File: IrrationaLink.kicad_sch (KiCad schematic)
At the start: 27 parts, among them J1 USB_C_Receptacle_USB2.0, U1 ESP32-C3, U2 LM2937xMP

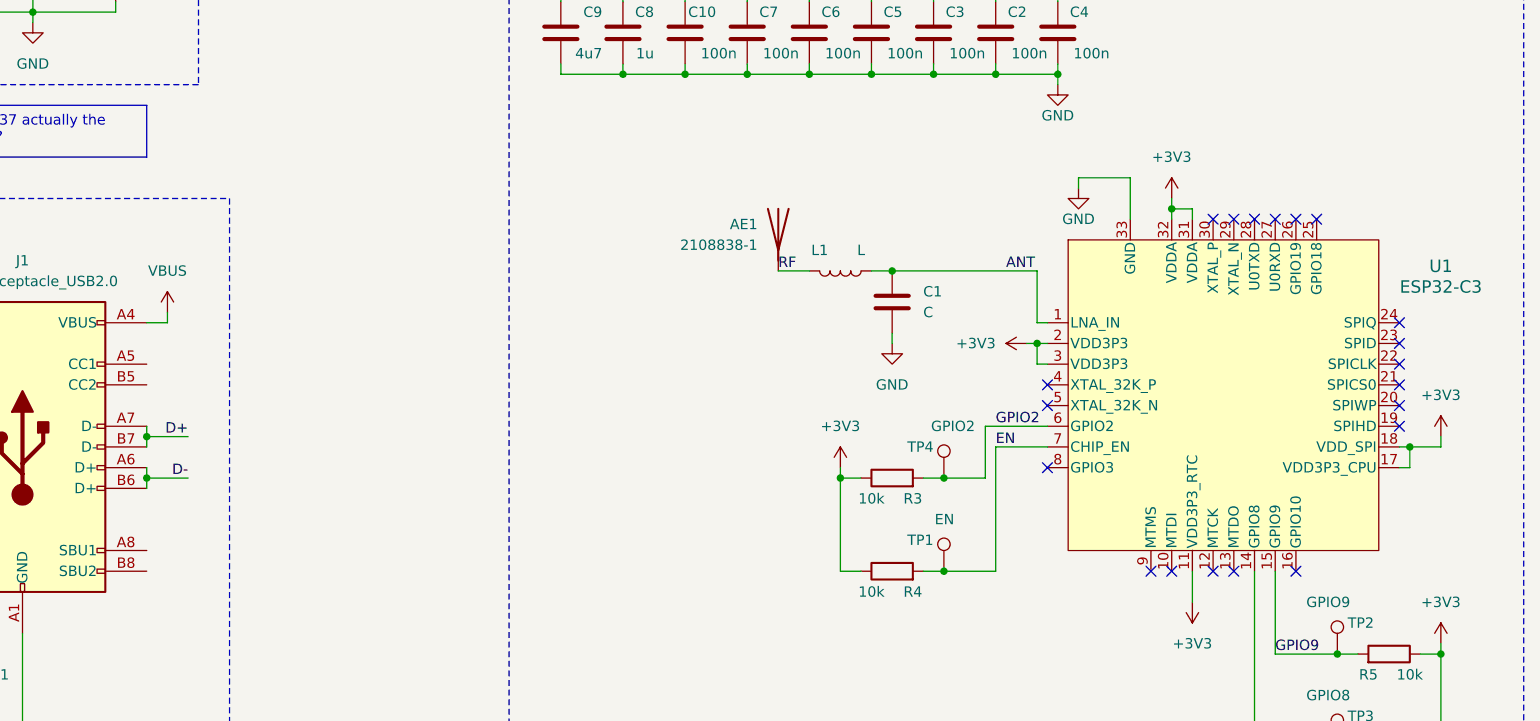
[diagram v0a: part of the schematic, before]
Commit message: Add gitignore; Route USB lines
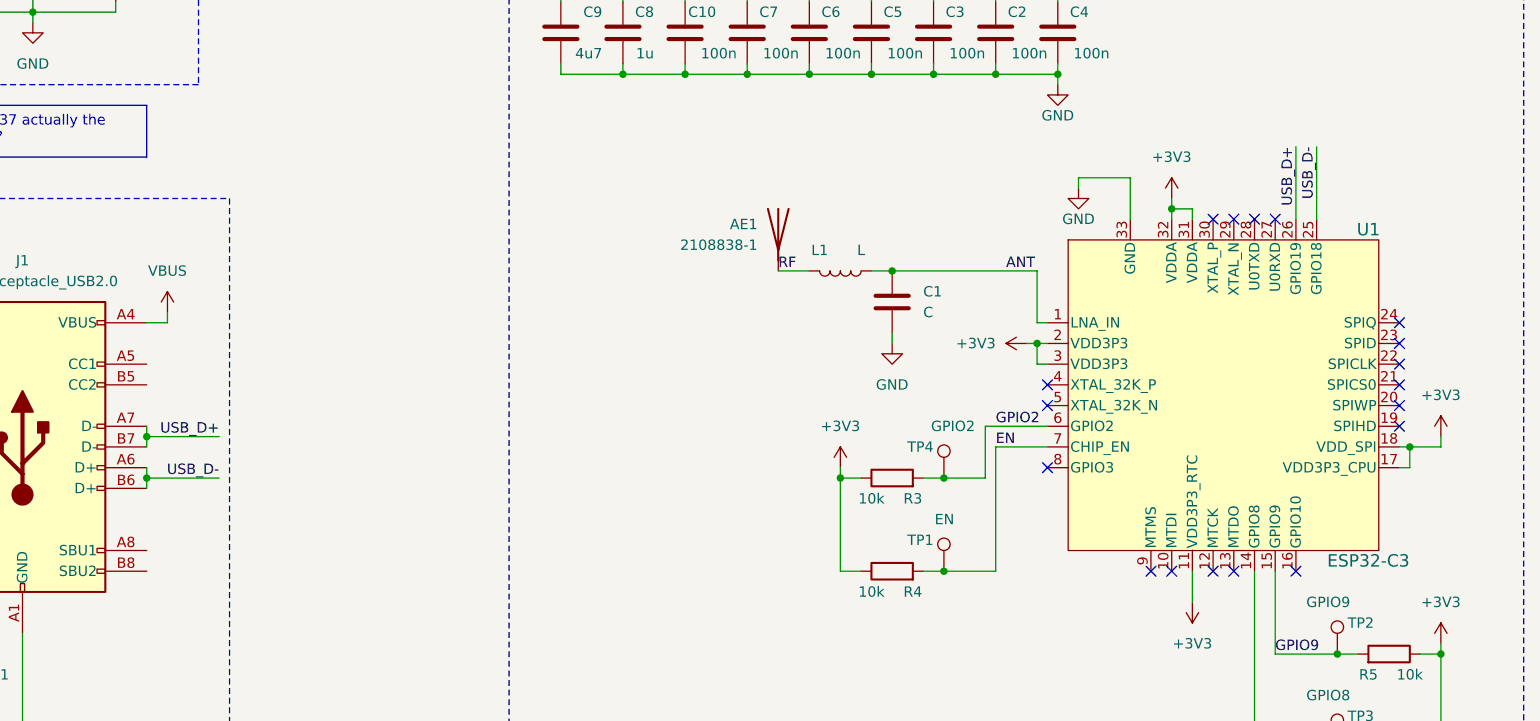
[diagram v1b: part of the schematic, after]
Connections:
- net D+ is gone; now on net USB_D+: J1.A7 (D-), J1.B7 (D-)
- net D- is gone; now on net USB_D-: J1.A6 (D+), J1.B6 (D+)
- net USB_D-: now reaches U1.25 (GPIO18)
- net USB_D+: now reaches U1.26 (GPIO19)
- no-connect marks 20 -> 18
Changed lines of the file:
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@@
   )
   (no_connect (at 233.68 86.36))
-  (no_connect (at 220.98 71.12))
   (no_connect (at 205.74 114.3))
   (no_connect (at 233.68 91.44))
@@
   (no_connect (at 190.5 93.98))
   (no_connect (at 233.68 83.82))
-  (no_connect (at 223.52 71.12))
   (wire (pts (xy 161.29 43.18) (xy 161.29 44.45))
     (stroke (width 0) (type default))
@@
     (stroke (width 0) (type default))
   )
-  (wire (pts (xy 80.01 102.87) (xy 85.09 102.87))
+  (wire (pts (xy 80.01 102.87) (xy 88.9 102.87))
     (stroke (width 0) (type default))
   )
@@
     (stroke (width 0) (type default))
   )
-  (wire (pts (xy 80.01 97.79) (xy 85.09 97.79))
+  (wire (pts (xy 80.01 97.79) (xy 88.9 97.79))
     (stroke (width 0) (type default))
   )
@@
     (stroke (width 0) (type default))
   )
+  (wire (pts (xy 223.52 62.23) (xy 223.52 71.12))
+    (stroke (width 0) (type default))
+  )
   (wire (pts (xy 146.05 43.18) (xy 138.43 43.18))
     (stroke (width 0) (type default))
@@
   )
   (wire (pts (xy 55.88 45.72) (xy 66.04 45.72))
+    (stroke (width 0) (type default))
+  )
+  (wire (pts (xy 220.98 62.23) (xy 220.98 71.12))
     (stroke (width 0) (type default))
   )
@@
     (effects (font (size 1.27 1.27)) (justify left bottom))
   )
-  (label "D-" (at 85.09 102.87 180) (fields_autoplaced)
+  (label "USB_D-" (at 88.9 102.87 180) (fields_autoplaced)
     (effects (font (size 1.27 1.27)) (justify right bottom))
   )
@@
     (effects (font (size 1.27 1.27)) (justify left bottom))
   )
-  (label "D+" (at 85.09 97.79 180) (fields_autoplaced)
+  (label "USB_D+" (at 88.9 97.79 180) (fields_autoplaced)
     (effects (font (size 1.27 1.27)) (justify right bottom))
   )
@@
     (effects (font (size 1.27 1.27)) (justify right bottom))
   )
+  (label "USB_D+" (at 220.98 62.23 270) (fields_autoplaced)
+    (effects (font (size 1.27 1.27)) (justify right bottom))
+  )
   (label "ANT" (at 185.42 77.47 0) (fields_autoplaced)
     (effects (font (size 1.27 1.27)) (justify left bottom))
+  )
+  (label "USB_D-" (at 223.52 62.23 270) (fields_autoplaced)
+    (effects (font (size 1.27 1.27)) (justify right bottom))
   )
   (label "GPIO9" (at 218.44 124.46 0) (fields_autoplaced)
@@
   )
   (symbol (lib_id "encyclopedia_galactica:ESP32-C3") (at 212.09 92.71 0) (unit 1)
-    (in_bom yes) (on_board yes) (dnp no) (fields_autoplaced)
-    (property "Reference" "U1" (at 238.76 76.8919 0)
+    (in_bom yes) (on_board yes) (dnp no)
+    (property "Reference" "U1" (at 229.87 72.39 0)
       (effects (font (size 1.524 1.524)))
     )
-    (property "Value" "ESP32-C3" (at 238.76 79.4319 0)
+    (property "Value" "ESP32-C3" (at 229.87 113.03 0)
       (effects (font (size 1.524 1.524)))
     )
@@
       (effects (font (size 1.27 1.27) italic) hide)
     )
-    (property "Datasheet" "ESP32-C3" (at 212.09 41.91 0)
+    (property "Datasheet" "https://www.espressif.com/sites/default/files/documentation/esp32-c3_datasheet_en.pdf" (at 212.09 41.91 0)
       (effects (font (size 1.27 1.27) italic) hide)
     )

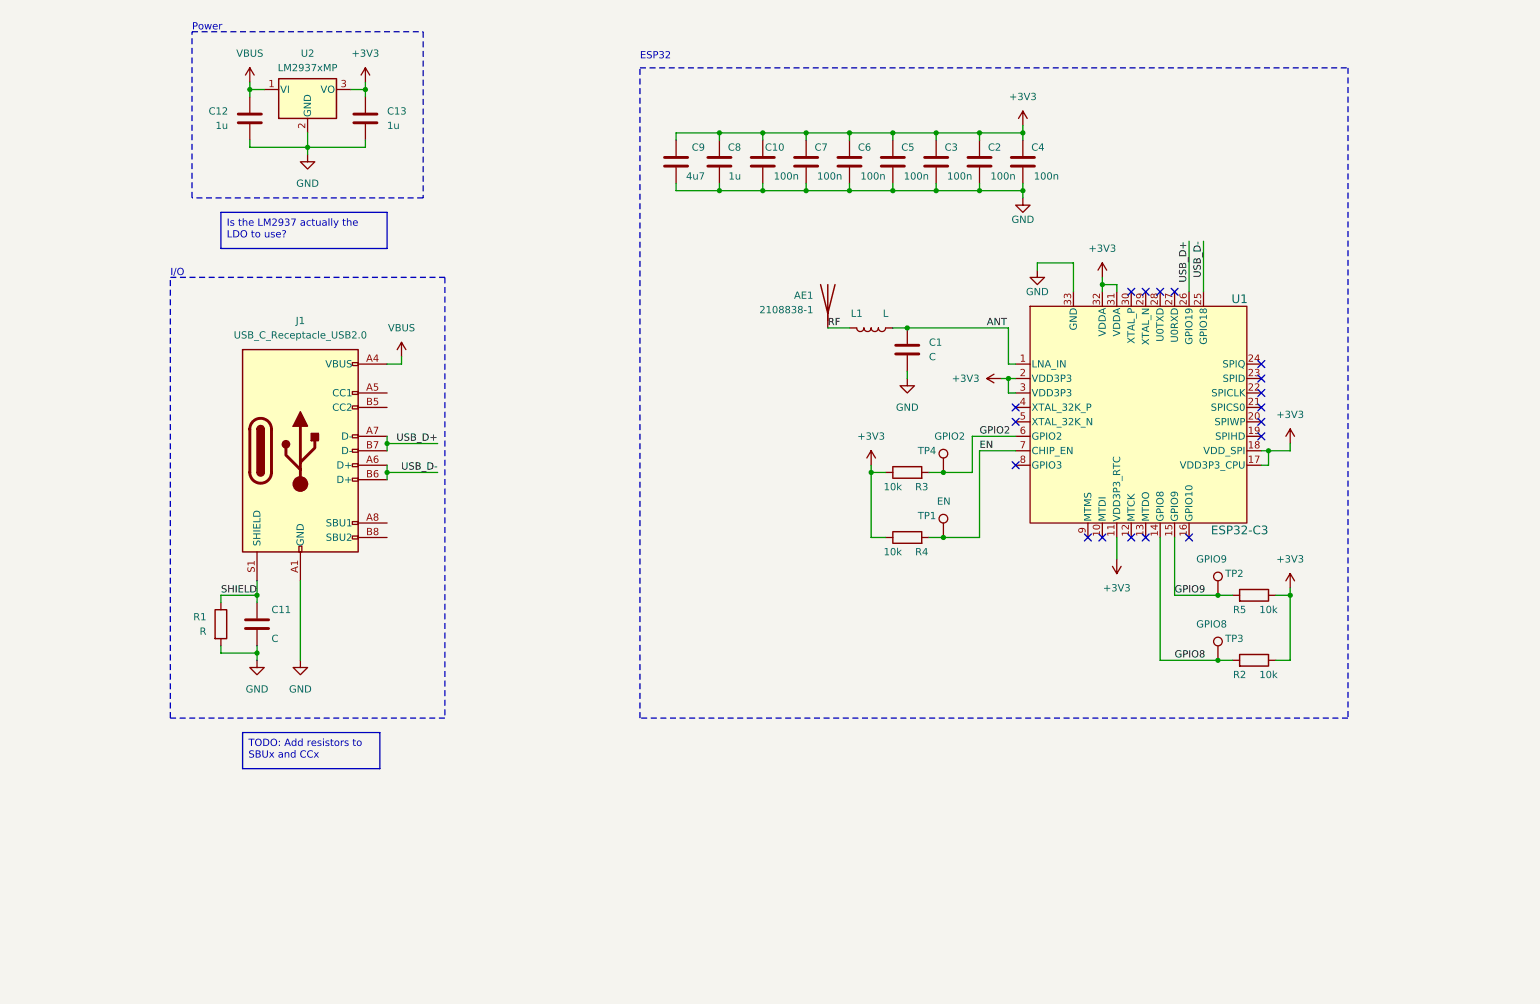
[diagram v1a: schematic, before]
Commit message: Design first version of board (Crystal not routed yet)
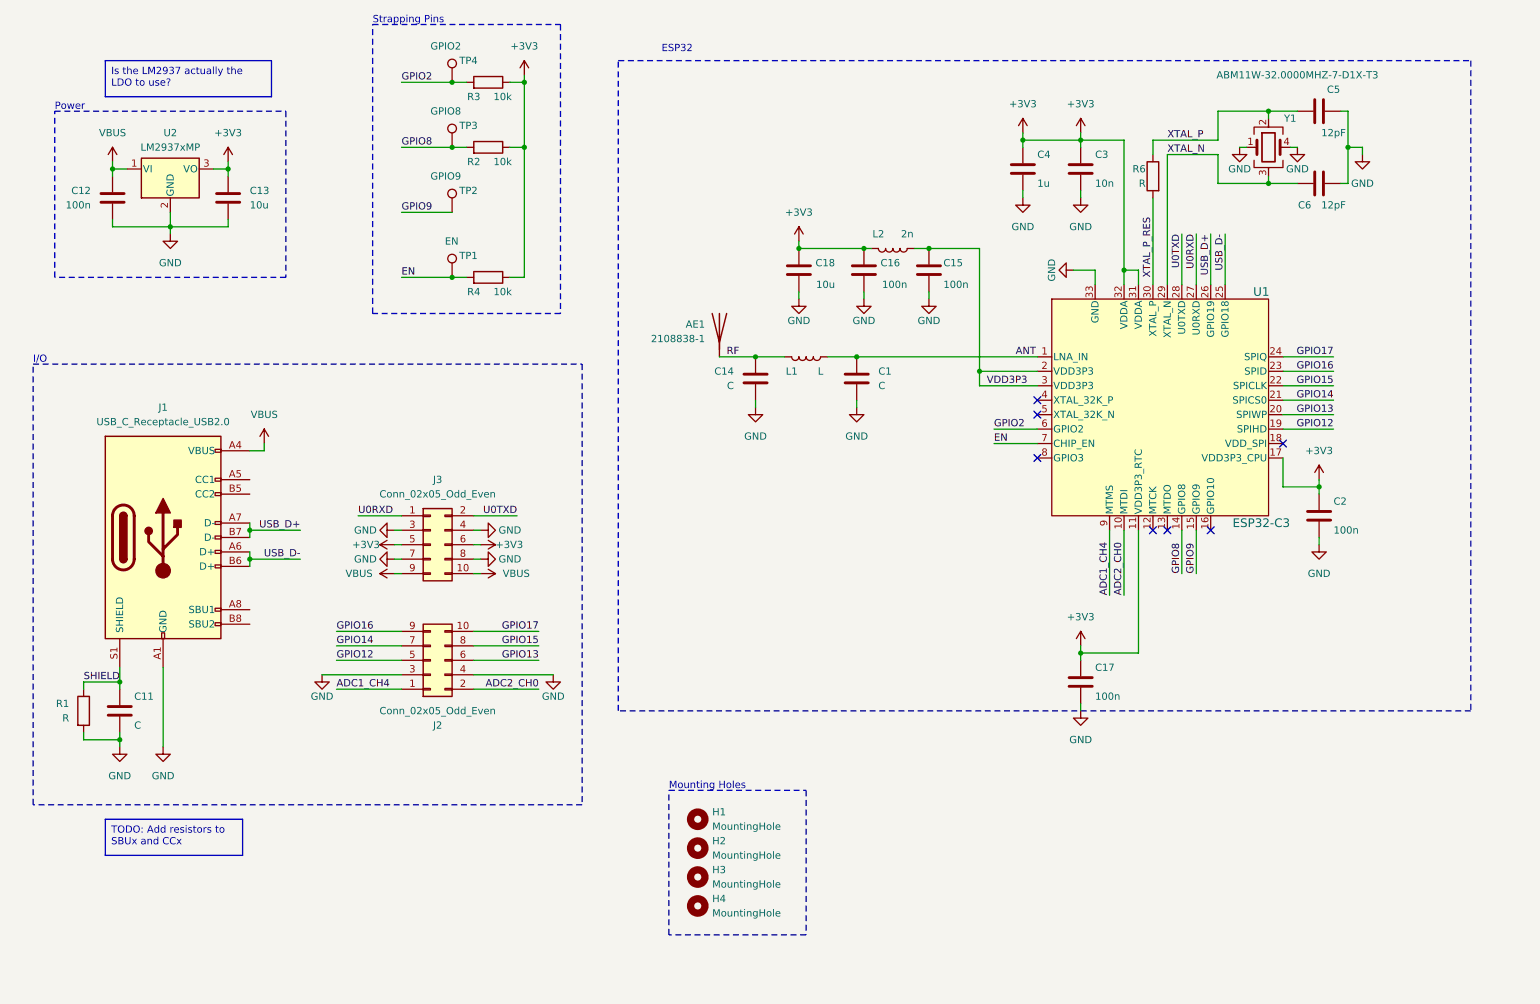
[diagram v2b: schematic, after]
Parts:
- removed C10, C7: 100n, Capacitor_SMD:C_0603_1608Metric, symbol Device:C
- removed C8: 1u, Capacitor_SMD:C_0603_1608Metric, symbol Device:C
- removed C9: 4u7, Capacitor_SMD:C_0603_1608Metric, symbol Device:C
- removed R5: 10k, Resistor_SMD:R_0603_1608Metric, symbol Device:R
- added C14: C, Capacitor_SMD:C_0402_1005Metric, symbol Device:C
- added C15, C16, C17: 100n, Capacitor_SMD:C_0402_1005Metric, symbol Device:C
- added C18: 10u, Capacitor_SMD:C_0603_1608Metric, symbol Device:C
- added H1, H2, H3, H4: MountingHole, MountingHole:MountingHole_2.2mm_M2, symbol Mechanical:MountingHole
- added J2, J3: Conn_02x05_Odd_Even, Connector_PinHeader_2.54mm:PinHeader_2x05_P2.54mm_Vertical, symbol Connector_Generic:Conn_02x05_Odd_Even
- added L2: 2n, Inductor_SMD:L_0402_1005Metric, symbol Device:L
- added R6: R, Resistor_SMD:R_0402_1005Metric, symbol Device:R
- added Y1: ABM11W-32.0000MHZ-7-D1X-T3, encyclopedia_galactica:ABM11W-30.0000MHZ-7-D1X-T3, symbol Device:Crystal_GND23
- C1, C11, C2: footprint Capacitor_SMD:C_0603_1608Metric -> Capacitor_SMD:C_0402_1005Metric
- C12: value 1u -> 100n; footprint Capacitor_SMD:C_0603_1608Metric -> Capacitor_SMD:C_0402_1005Metric
- C13: value 1u -> 10u
- C3: value 100n -> 10n; footprint Capacitor_SMD:C_0603_1608Metric -> Capacitor_SMD:C_0402_1005Metric
- C4: value 100n -> 1u; footprint Capacitor_SMD:C_0603_1608Metric -> Capacitor_SMD:C_0402_1005Metric
- C5, C6: value 100n -> 12pF; footprint Capacitor_SMD:C_0603_1608Metric -> Capacitor_SMD:C_0402_1005Metric
- L1: footprint Inductor_SMD:L_0603_1608Metric -> Inductor_SMD:L_0402_1005Metric
- R1, R2, R3, R4: footprint Resistor_SMD:R_0603_1608Metric -> Resistor_SMD:R_0402_1005Metric
- TP1, TP2, TP3, TP4: footprint TestPoint:TestPoint_Pad_D2.0mm -> TestPoint:TestPoint_Pad_D1.5mm
- U1: HW_Guidelines (none) -> https://www.espressif.com/sites/default/files/documentation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
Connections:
- net +3V3: now also C16.1, C17.1, C18.1, J3.5 (Pin_5), J3.6 (Pin_6), L2.1; no longer C5.1, C6.1, U1.18 (VDD_SPI), U1.2 (VDD3P3), U1.3 (VDD3P3)
- net GND: now also C14.2, C15.2, C16.2, C17.2, C18.2, J2.3 (Pin_3), J2.4 (Pin_4), J3.3 (Pin_3), J3.4 (Pin_4), J3.7 (Pin_7), J3.8 (Pin_8), Y1.1, Y1.4
- net RF: now also C14.1
- net VBUS: now also J3.10 (Pin_10), J3.9 (Pin_9)
- net ADC2_CH0: now reaches U1.10 (MTDI)
- net ADC2_CH0: now also J2.2 (Pin_2)
- net GPIO12: now reaches U1.19 (SPIHD)
- net GPIO12: now also J2.5 (Pin_5)
- net GPIO13: now reaches U1.20 (SPIWP)
- net GPIO13: now also J2.6 (Pin_6)
- net GPIO14: now reaches U1.21 (SPICS0)
- net GPIO14: now also J2.7 (Pin_7)
- net GPIO15: now reaches U1.22 (SPICLK)
- net GPIO15: now also J2.8 (Pin_8)
- net GPIO16: now reaches U1.23 (SPID)
- net GPIO16: now also J2.9 (Pin_9)
- net GPIO17: now reaches U1.24 (SPIQ)
- net GPIO17: now also J2.10 (Pin_10)
- net U0RXD: now reaches U1.27 (U0RXD)
- net U0RXD: now also J3.1 (Pin_1)
- net U0TXD: now reaches U1.28 (U0TXD)
- net U0TXD: now also J3.2 (Pin_2)
- net XTAL_N: now reaches U1.29 (XTAL_N)
- net XTAL_N: now also C6.1, Y1.3
- net XTAL_P_RES: now reaches U1.30 (XTAL_P)
- net XTAL_P_RES: now also R6.2
- net ADC1_CH4: now reaches U1.9 (MTMS)
- net ADC1_CH4: now also J2.1 (Pin_1)
- new net VDD3P3: C15.1, L2.2, U1.2 (VDD3P3), U1.3 (VDD3P3)
- new net XTAL_P: C5.1, R6.1, Y1.2
- no-connect marks 18 -> 7
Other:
- note added: "Mounting Holes"
- note added: "Strapping Pins"
- moved on the sheet: AE1, C1, C11, C12, C13, J1, L1, R1, R2, R3, R4, TP1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

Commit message: Add button; Move power lines
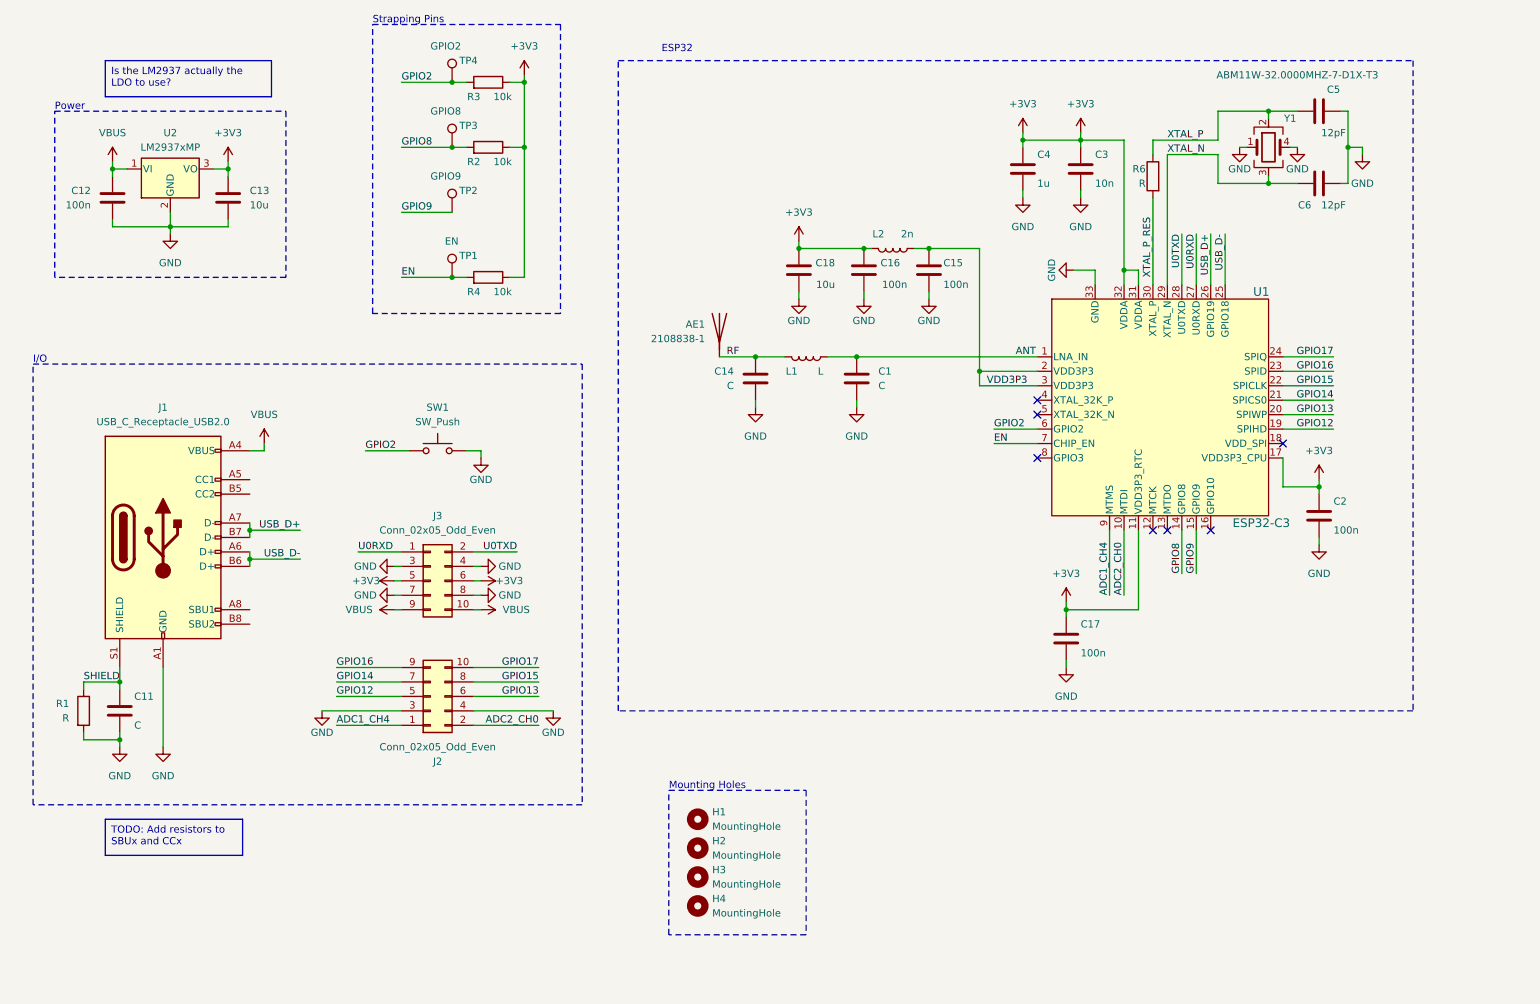
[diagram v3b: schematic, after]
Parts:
- added SW1: SW_Push, Button_Switch_SMD:SW_SPST_B3U-1000P, symbol Switch:SW_Push
- C11: footprint Capacitor_SMD:C_0402_1005Metric -> Capacitor_SMD:C_0603_1608Metric
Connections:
- net GND: now also SW1.1
- net GPIO2: now also SW1.2
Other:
- moved on the sheet: C17, J2, J3
